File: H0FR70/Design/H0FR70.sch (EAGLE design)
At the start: 36 parts, among them P1 HEXABIT_17.32_NO_P6, Q1 BSS123, Q2 STD36P4LLF6, U2 INA199A2DCKT, X1 XTALL_CSTCE8M00G52

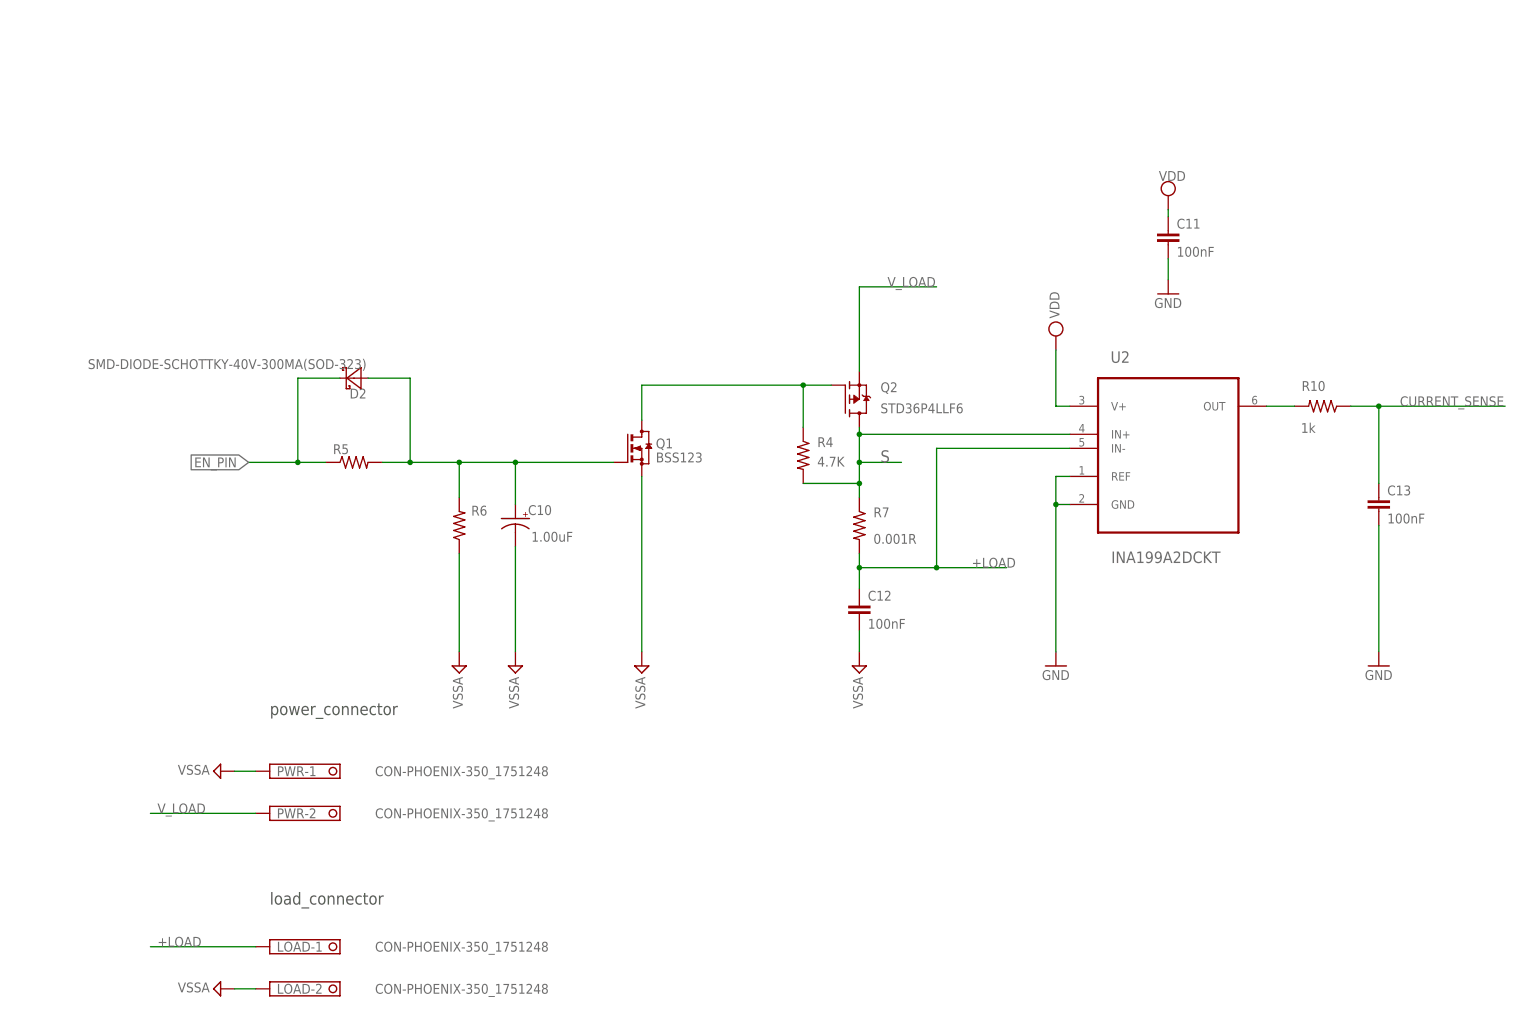
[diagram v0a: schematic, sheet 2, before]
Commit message: current sense pin connnected to PA0 (ADC_IN0) Orange indicator led in parallel with load remove power pads at top adding lables & notes
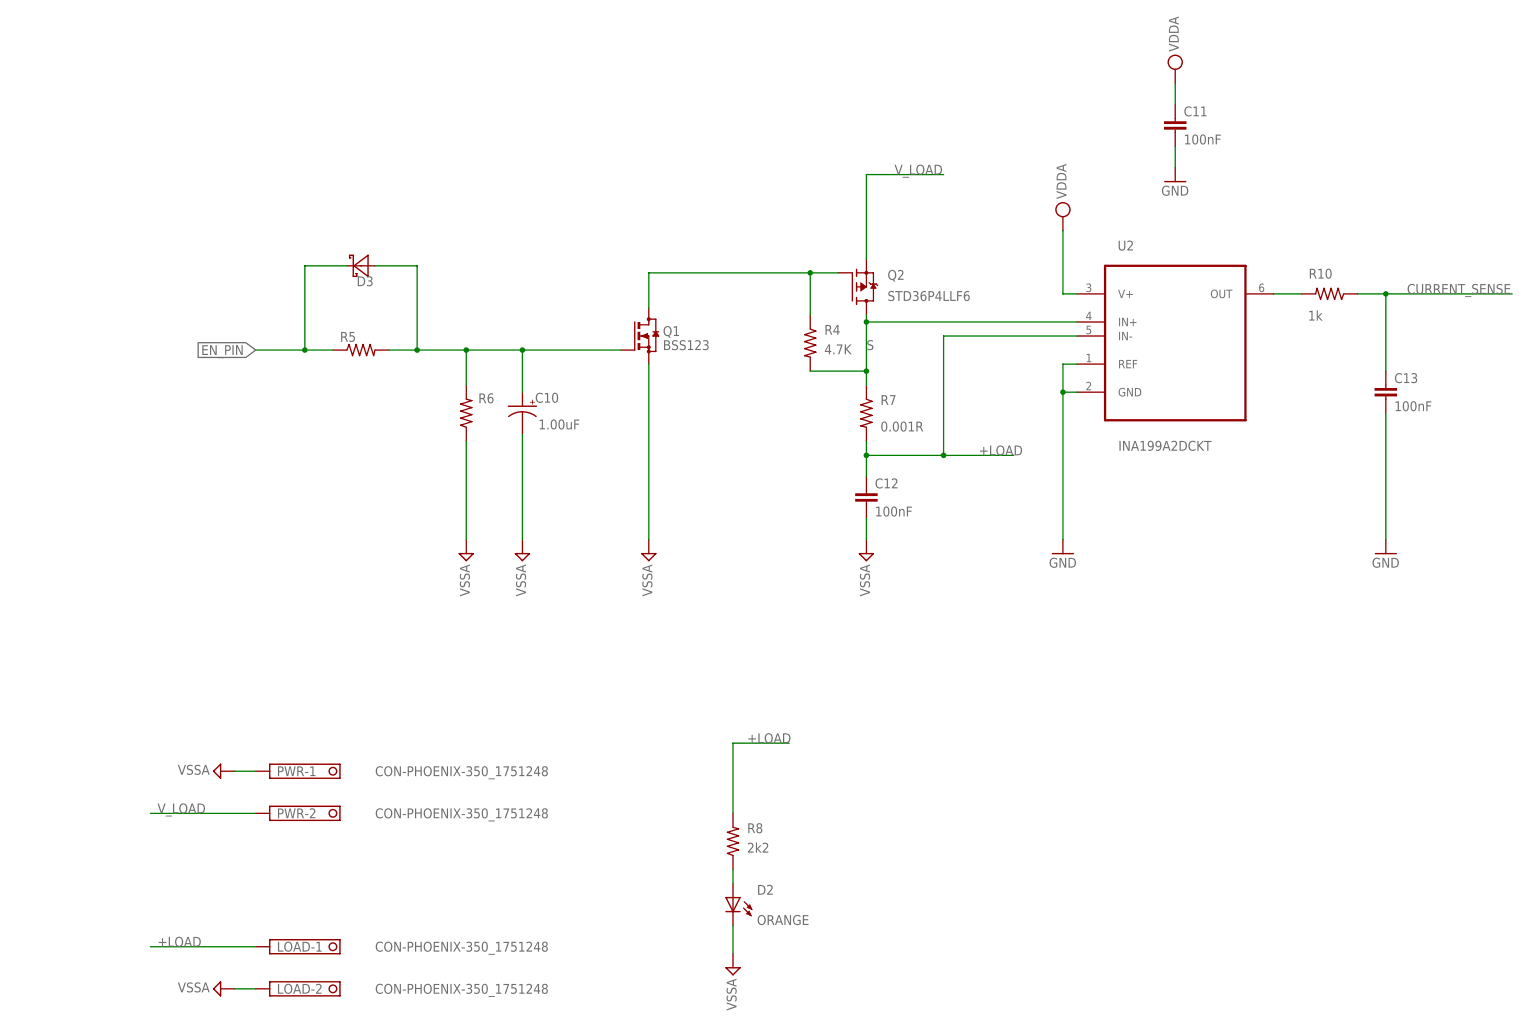
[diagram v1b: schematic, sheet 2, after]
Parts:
- removed P1: HEXABIT_17.32_NO_P6, hexabitz_connectors:HEXABIT_17.32_NO_P6
- added D3: SMD-DIODE-SCHOTTKY-40V-300MA(SOD-323), Hexabitz:SMD-DIODE-SCHOTTKY-40V-300MA(SOD-323)
- added P2: HEXABIT_17.32_NO_P6_P7_P12, hexabitz_connectors:HEXABIT_17.32_NO_P6_P7_P12
- added R8: 2k2, Hexabitz:R-0603
- D2: value SMD-DIODE-SCHOTTKY-40V-300MA(SOD-323) -> ORANGE; device Hexabitz:SMD-DIODE-SCHOTTKY-40V-300MA(SOD-323) -> Hexabitz:VLMS1300-GS08; MFN (none) -> Vishay; MPN (none) -> VLMO1300-GS08; OCTOPART_URL (none) -> https://octopart.com/vlmo1300-gs08-vishay-21709200?r=sp#
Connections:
- new net N$8: D2.A, R8.1
- net +LOAD: now also R8.2
- net AGND: now also D2.C
- net CURRENT_SENSE: now also U1.PA0
- net EN_PIN: now also D3.C; no longer D2.C
- net GND: now also P2.GND2, P2.GND3, P2.GND4, P2.GND5, U1.PA15; no longer P1.GND1, P1.GND2, P1.GND3, P1.GND4, P1.GND5, P1.GND6
- net N$13: now also D3.A; no longer D2.A
- net UART1_RX: now also P2.SD5; no longer P1.SD5
- net UART1_TX: now also P2.SU5; no longer P1.SU5
- net UART2_RX: now also P2.SD2; no longer P1.SD2
- net UART2_TX: now also P2.SU2; no longer P1.SU2
- net UART3_RX: now also P2.SD4; no longer P1.SD4
- net UART3_TX: now also P2.SU4; no longer P1.SU4
- net UART5_RX: now also P2.SD1; no longer P1.SD1
- net UART5_TX: now also P2.SU1; no longer P1.SU1
- net UART6_RX: now also P2.SD3; no longer P1.SD3
- net UART6_TX: now also P2.SU3; no longer P1.SU3
- net VDD: now also P2.VDD2, P2.VDD3, P2.VDD4, P2.VDD5; no longer C11.1, P1.VDD1, P1.VDD2, P1.VDD3, P1.VDD4, P1.VDD5, P1.VDD6, U2.V+
- net VDDA: now also C11.1, U2.V+
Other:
- note added: "SPST MOSFET Switch upto 20A 40V"
- note removed: "SPST MOSFET Switch Module"
- moved on the sheet: C10, C11, C12, C13, Q1, Q2, R10, R4, R5, R6, R7, U2

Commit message: fix a bug in schematics
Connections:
- net S: no longer R4.2
- net V_LOAD: now also R4.2
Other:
- moved on the sheet: R4
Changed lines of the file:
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@@
 <attribute name="VALUE" x="62.23" y="18.161" size="1.778" layer="96"/>
 </instance>
-<instance part="R4" gate="G$1" x="140.97" y="135.89" smashed="yes" rot="R270">
-<attribute name="NAME" x="143.51" y="137.3886" size="1.778" layer="95"/>
-<attribute name="VALUE" x="143.51" y="133.858" size="1.778" layer="96"/>
+<instance part="R4" gate="G$1" x="140.97" y="156.21" smashed="yes" rot="R90">
+<attribute name="NAME" x="138.43" y="154.7114" size="1.778" layer="95" rot="R180"/>
+<attribute name="VALUE" x="138.43" y="158.242" size="1.778" layer="96" rot="R180"/>
 </instance>
 <instance part="Q1" gate="G$1" x="111.76" y="137.16" smashed="yes">
@@
 <wire x1="111.76" y1="148.59" x2="140.97" y2="148.59" width="0.1524" layer="91"/>
 <pinref part="R4" gate="G$1" pin="1"/>
-<wire x1="140.97" y1="140.97" x2="140.97" y2="148.59" width="0.1524" layer="91"/>
+<wire x1="140.97" y1="151.13" x2="140.97" y2="148.59" width="0.1524" layer="91"/>
 <junction x="140.97" y="148.59"/>
 <pinref part="Q2" gate="G$1" pin="G"/>
@@
 <net name="S" class="0">
 <segment>
-<pinref part="R4" gate="G$1" pin="2"/>
-<wire x1="140.97" y1="130.81" x2="151.13" y2="130.81" width="0.1524" layer="91"/>
-<wire x1="151.13" y1="130.81" x2="151.13" y2="139.7" width="0.1524" layer="91"/>
+<wire x1="151.13" y1="128.27" x2="151.13" y2="139.7" width="0.1524" layer="91"/>
 <wire x1="151.13" y1="139.7" x2="151.13" y2="140.97" width="0.1524" layer="91"/>
-<wire x1="151.13" y1="130.81" x2="151.13" y2="128.27" width="0.1524" layer="91"/>
-<junction x="151.13" y="130.81"/>
 <pinref part="Q2" gate="G$1" pin="D"/>
 <wire x1="151.13" y1="139.7" x2="189.23" y2="139.7" width="0.1524" layer="91"/>
@@
 <pinref part="Q2" gate="G$1" pin="S"/>
 <label x="156.21" y="166.37" size="1.778" layer="95"/>
-<wire x1="151.13" y1="166.37" x2="151.13" y2="151.13" width="0.1524" layer="91"/>
+<wire x1="151.13" y1="166.37" x2="151.13" y2="163.83" width="0.1524" layer="91"/>
+<wire x1="151.13" y1="163.83" x2="151.13" y2="151.13" width="0.1524" layer="91"/>
 <wire x1="151.13" y1="166.37" x2="165.1" y2="166.37" width="0.1524" layer="91"/>
-</segment>
-<segment>
+<pinref part="R4" gate="G$1" pin="2"/>
+<wire x1="140.97" y1="161.29" x2="140.97" y2="163.83" width="0.1524" layer="91"/>
+<wire x1="140.97" y1="163.83" x2="151.13" y2="163.83" width="0.1524" layer="91"/>
+<junction x="151.13" y="163.83"/>
+</segment>
+<segment>
